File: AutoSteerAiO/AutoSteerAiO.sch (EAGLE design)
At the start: 84 parts, among them K4 CB1A-P-12V, T1 BC547, U1 VX7805-1000

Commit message: Add files via upload
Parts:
- IBT2: device SparkFun-Connectors:CONN_04X2 -> pinhead:PINHD-2X4
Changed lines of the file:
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@@
 <?xml version="1.0" encoding="utf-8"?>
 <!DOCTYPE eagle SYSTEM "eagle.dtd">
-<eagle version="9.3.2">
+<eagle version="9.4.0">
 <drawing>
 <settings>
@@
 <attribute name="OC_NEWARK" value="unknown"/>
 </part>
-<part name="IBT2" library="SparkFun-Connectors" library_urn="urn:adsk.eagle:library:513" deviceset="CONN_04X2" device="" package3d_urn="urn:adsk.eagle:package:38103/1">
+<part name="IBT2" library="pinhead" library_urn="urn:adsk.eagle:library:325" deviceset="PINHD-2X4" device="" package3d_urn="urn:adsk.eagle:package:22461/2">
 <attribute name="MF" value=""/>
 <attribute name="MPN" value=""/>
@@
 <attribute name="MPN" x="73.66" y="270.51" size="1.778" layer="96" display="off"/>
 </instance>
-<instance part="IBT2" gate="G$1" x="53.34" y="99.06" smashed="yes">
+<instance part="IBT2" gate="A" x="53.34" y="99.06" smashed="yes">
 <attribute name="VALUE" x="49.53" y="91.694" size="1.778" layer="96" font="vector"/>
 <attribute name="NAME" x="49.276" y="107.188" size="1.778" layer="95" font="vector"/>
@@
 </segment>
 <segment>
-<pinref part="IBT2" gate="G$1" pin="7"/>
-<wire x1="45.72" y1="96.52" x2="40.64" y2="96.52" width="0.1524" layer="91"/>
+<pinref part="IBT2" gate="A" pin="7"/>
+<wire x1="50.8" y1="96.52" x2="40.64" y2="96.52" width="0.1524" layer="91"/>
 <label x="40.64" y="96.52" size="1.778" layer="95"/>
 </segment>
@@
 </segment>
 <segment>
-<pinref part="IBT2" gate="G$1" pin="8"/>
-<wire x1="60.96" y1="96.52" x2="66.04" y2="96.52" width="0.1524" layer="91"/>
+<pinref part="IBT2" gate="A" pin="8"/>
+<wire x1="58.42" y1="96.52" x2="66.04" y2="96.52" width="0.1524" layer="91"/>
 <label x="60.96" y="96.52" size="1.778" layer="95"/>
 </segment>
@@
 </segment>
 <segment>
-<pinref part="IBT2" gate="G$1" pin="3"/>
-<wire x1="45.72" y1="101.6" x2="43.18" y2="101.6" width="0.1524" layer="91"/>
+<pinref part="IBT2" gate="A" pin="3"/>
+<wire x1="50.8" y1="101.6" x2="43.18" y2="101.6" width="0.1524" layer="91"/>
 <label x="43.18" y="101.6" size="1.778" layer="95"/>
 </segment>
 <segment>
-<pinref part="IBT2" gate="G$1" pin="4"/>
-<wire x1="60.96" y1="101.6" x2="63.5" y2="101.6" width="0.1524" layer="91"/>
+<pinref part="IBT2" gate="A" pin="4"/>
+<wire x1="58.42" y1="101.6" x2="63.5" y2="101.6" width="0.1524" layer="91"/>
 <label x="60.96" y="101.6" size="1.778" layer="95"/>
 </segment>
@@
 <net name="PWM1" class="0">
 <segment>
-<pinref part="IBT2" gate="G$1" pin="2"/>
-<wire x1="60.96" y1="104.14" x2="68.58" y2="104.14" width="0.1524" layer="91"/>
+<pinref part="IBT2" gate="A" pin="2"/>
+<wire x1="58.42" y1="104.14" x2="68.58" y2="104.14" width="0.1524" layer="91"/>
 <label x="60.96" y="104.14" size="1.778" layer="95"/>
 </segment>
@@
 <net name="PWM2" class="0">
 <segment>
-<pinref part="IBT2" gate="G$1" pin="1"/>
-<wire x1="45.72" y1="104.14" x2="38.1" y2="104.14" width="0.1524" layer="91"/>
+<pinref part="IBT2" gate="A" pin="1"/>
+<wire x1="50.8" y1="104.14" x2="38.1" y2="104.14" width="0.1524" layer="91"/>
 <label x="38.1" y="104.14" size="1.778" layer="95"/>
 </segment>

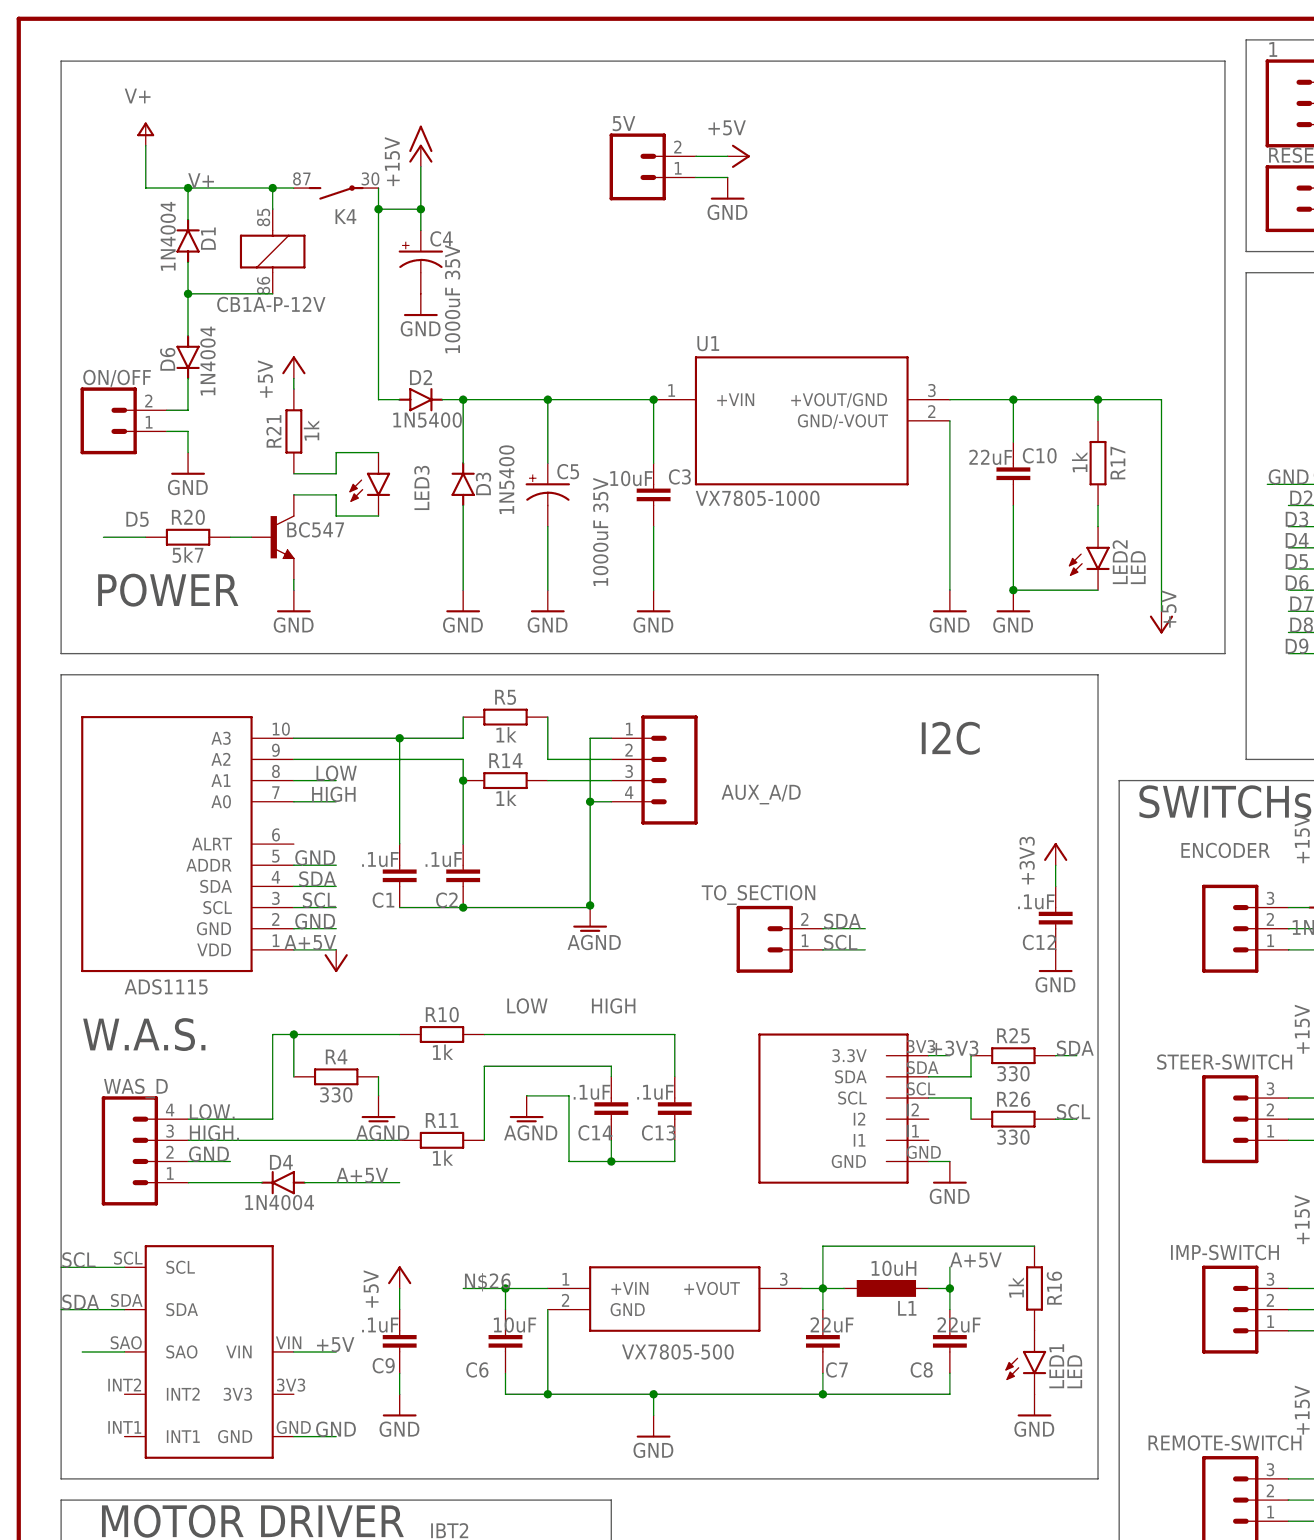
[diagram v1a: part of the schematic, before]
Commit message: Add files via upload
Added Led diode IMP, WORK and STEER
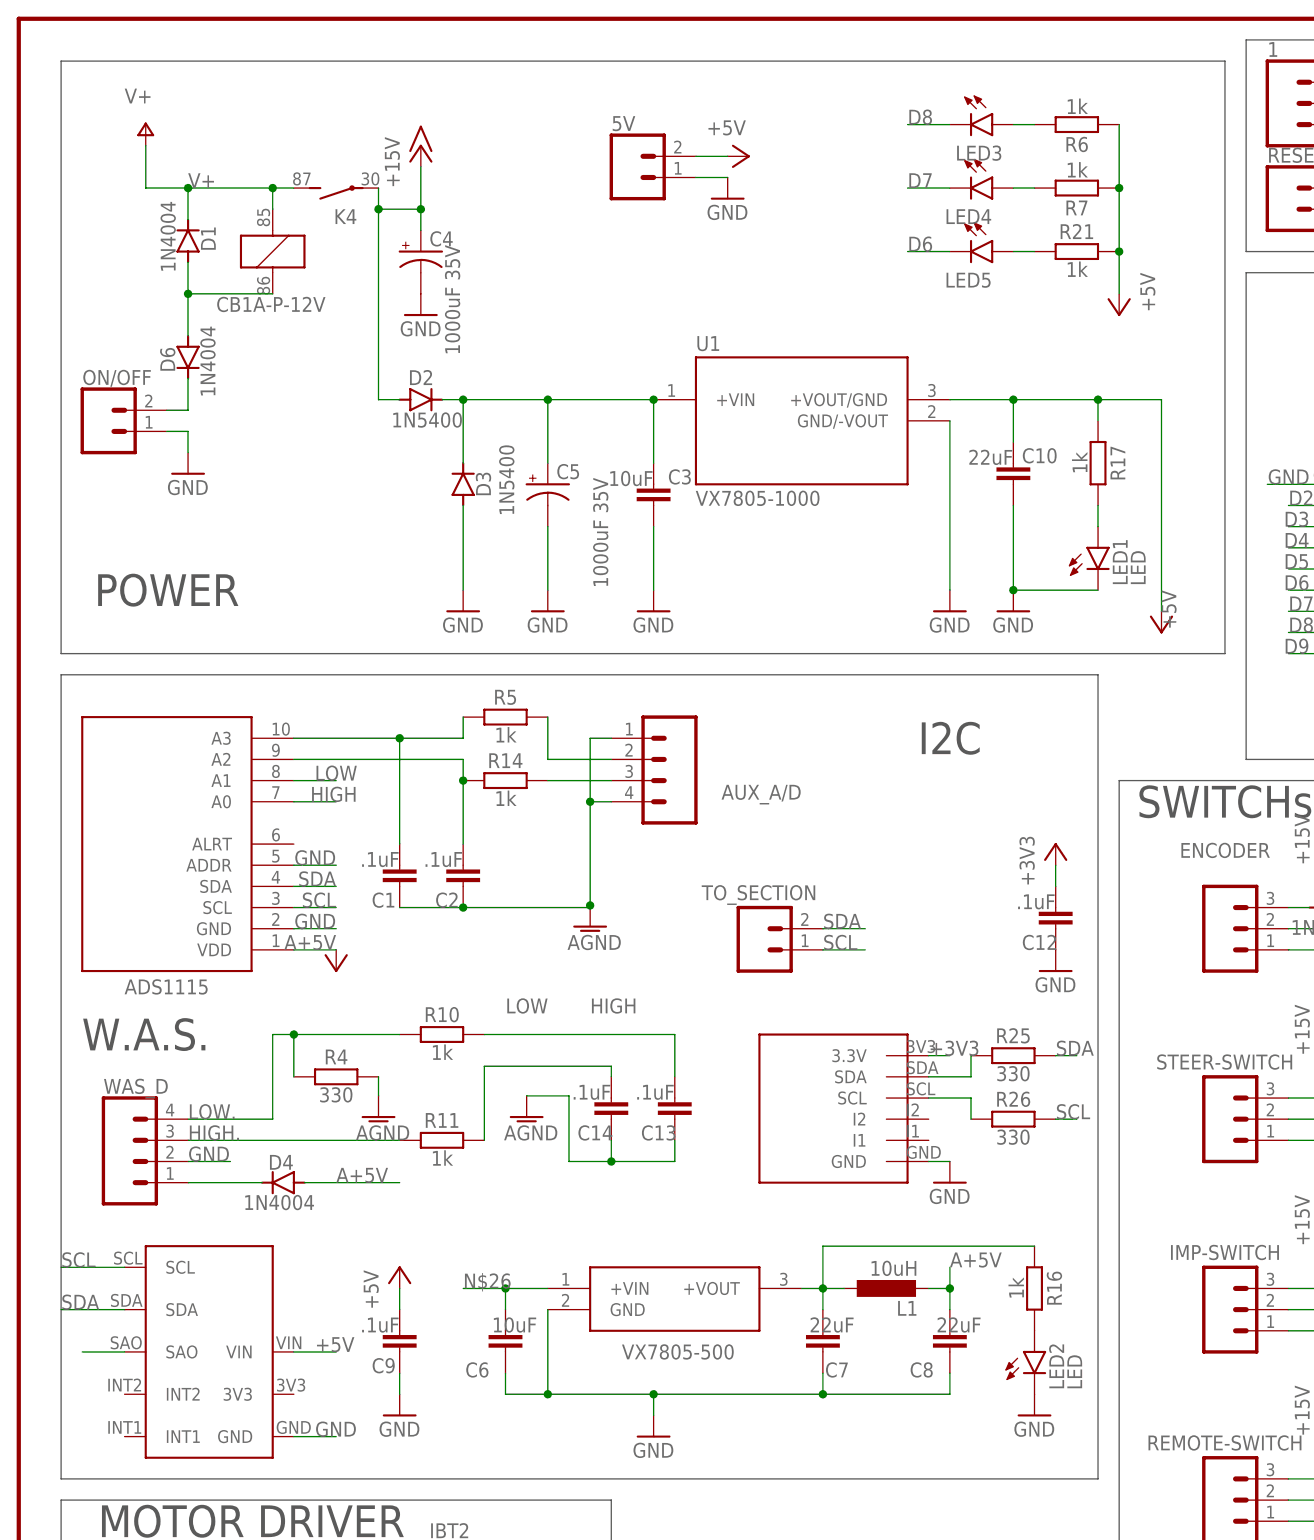
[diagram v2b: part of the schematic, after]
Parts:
- removed R20: 5k7, resistor:R-EU_0207/7
- removed T1: BC547, transistor:BC547
- added LED4, LED5: LED, led:LED3MM
- added R6, R7: 1k, resistor:R-EU_0207/7
- D1, D4, D5, D6: device diode:1N4004 -> #Diode 2:1N4004
- D2, D3: device diode:1N5400 -> #Diode 2:1N5400
- IBT2: device pinhead:PINHD-2X4 -> #pinhead:PINHD-2X4
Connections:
- removed net N$24: LED3.A, R21.1
- removed net N$27: LED3.C, T1.C
- new net N$22: LED3.A, R6.2
- new net N$31: LED4.A, R7.2
- net +5V: now also R6.1, R7.1
- net D5: no longer R20.1
- net D6: now also LED5.C
- net D7: now also LED4.C
- net D8: now also LED3.C
- net GND: no longer T1.E
- net N$13: now also LED2.A; no longer LED1.A
- net N$14: now also LED1.A; no longer LED2.A
- net N$23: now also LED5.A, R21.1; no longer R20.2, T1.B
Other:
- moved on the sheet: LED1, LED2, LED3, R21

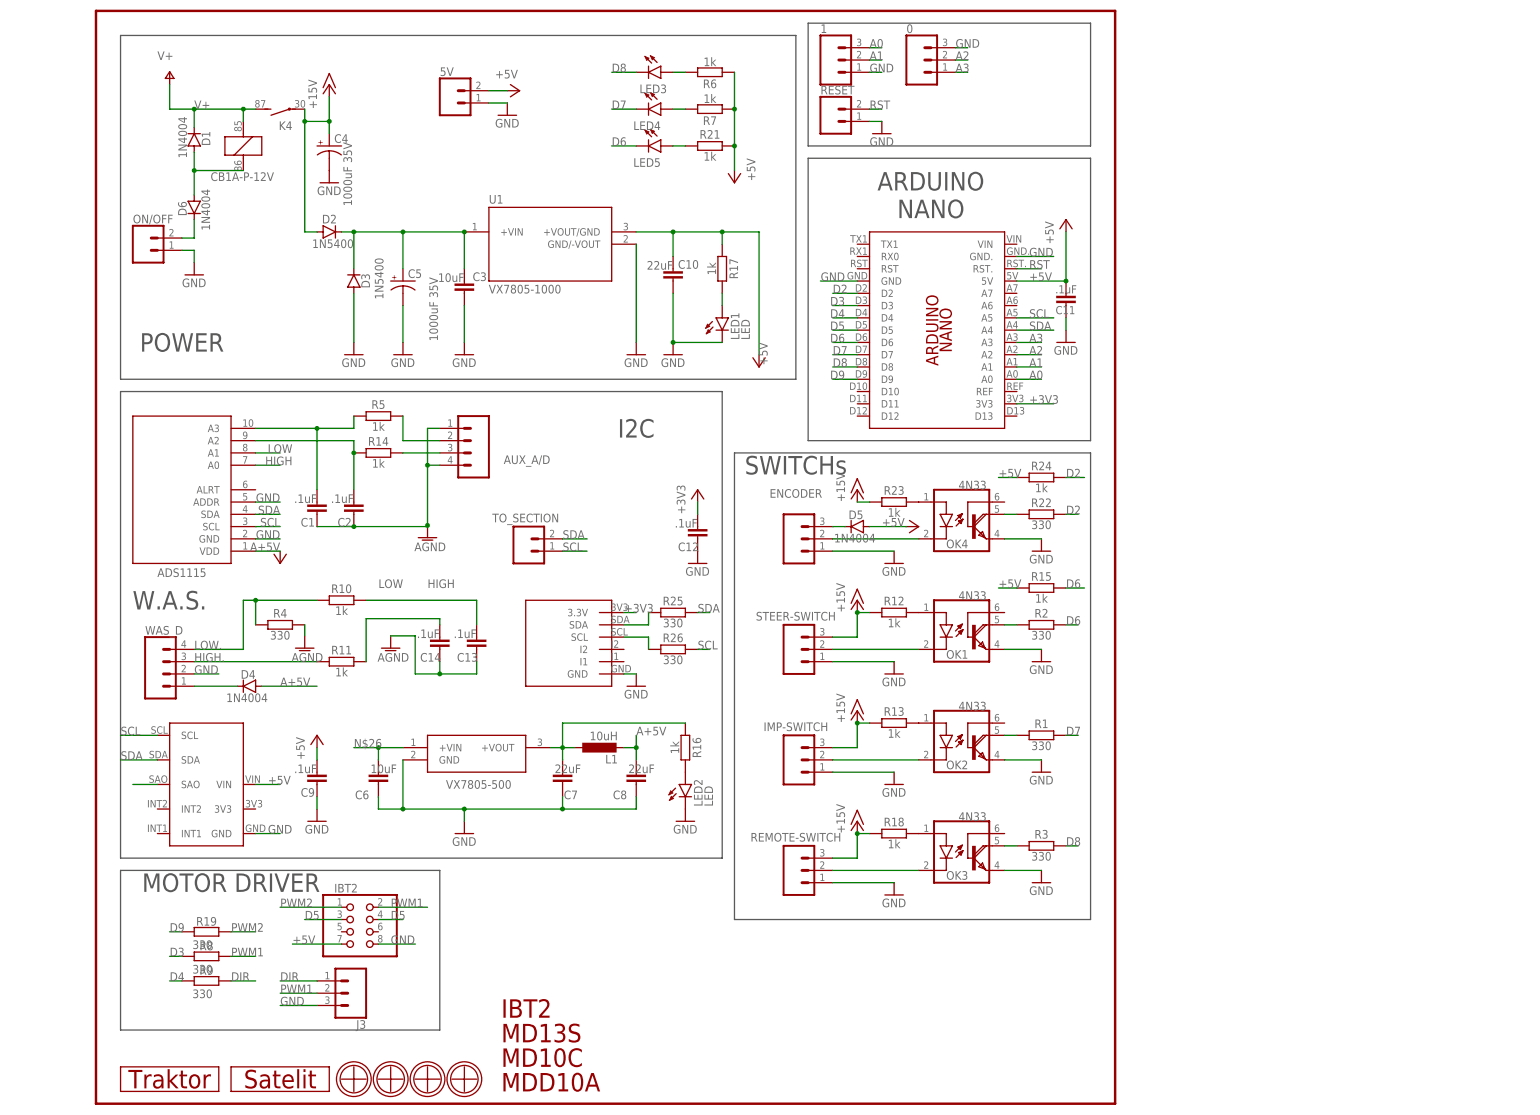
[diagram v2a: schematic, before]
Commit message: Add files via upload
replaced VX7805-500 with LM7805 - power supply for W.A.S.
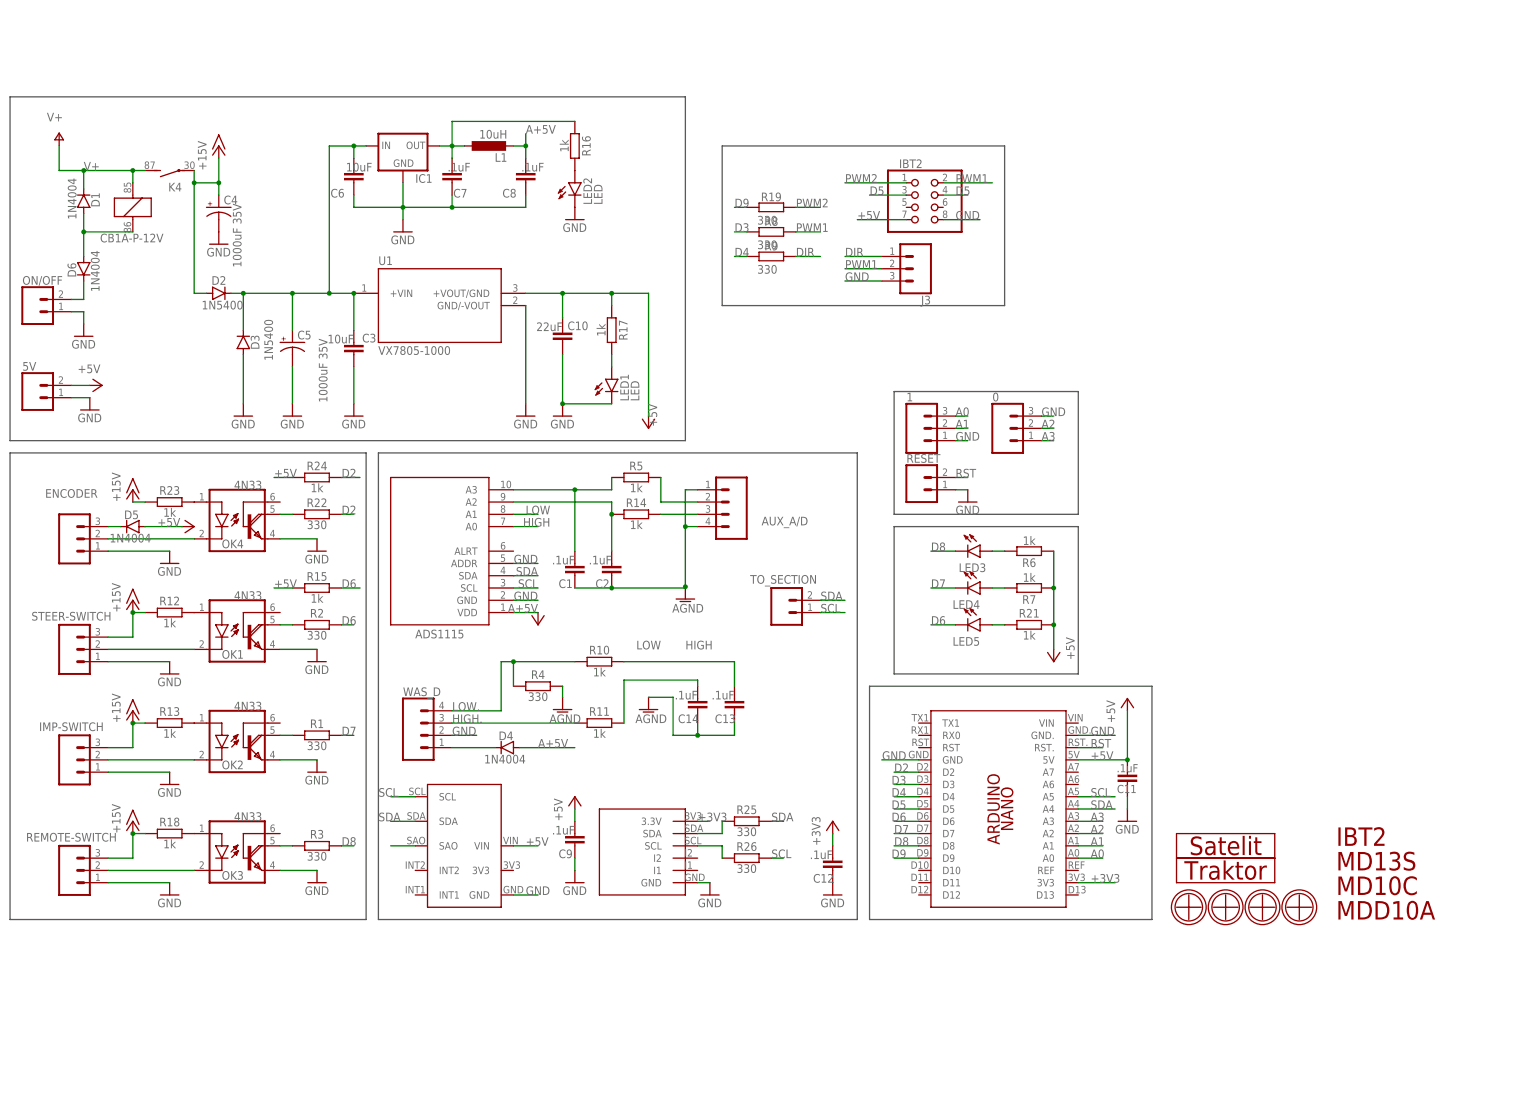
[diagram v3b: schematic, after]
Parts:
- removed PS1: VX7805-500, #VX7805-500:VX7805-500
- added IC1: (no value), v-reg:78XXS
- C7, C8: value 22uF -> .1uF
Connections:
- net GND: now also IC1.GND; no longer PS1.GND
- net N$25: now also IC1.OUT; no longer PS1.+VOUT
- net N$26: now also IC1.IN; no longer PS1.+VIN
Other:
- note removed: "ARDUINO NANO"
- note removed: "I2C"
- note removed: "MOTOR DRIVER"
- note removed: "POWER"
- note removed: "SWITCHs"
- note removed: "W.A.S."
- moved on the sheet: 0, 1, 5V, ADS1115, AUX_A/D, C1, C10, C11, C12, C13, C14, C2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

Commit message: Add files via upload
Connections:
- net N$21 renamed A+5V.
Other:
- moved on the sheet: 0, 1, C1, C11, C12, C13, C14, C2, C4, C9, D4, IBT2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

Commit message: Add files via upload
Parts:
- added C15: .1uF, resistor:C-EU050-024X044
- renumbered IC1 to 7805
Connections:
- net GND: now also C15.1
- net N$25: now also C15.2
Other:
- moved on the sheet: C7, C8, L1, LED2, R16
